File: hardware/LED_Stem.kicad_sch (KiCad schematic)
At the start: 4 parts

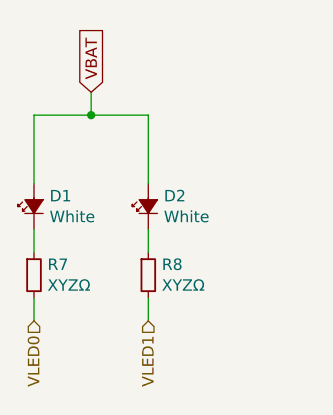
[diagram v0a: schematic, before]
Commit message: Fixed a bug, where I was sorting all the LEDs :S Removed all DRC rules Ready to fillet tracks
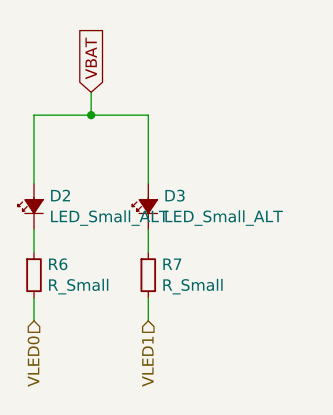
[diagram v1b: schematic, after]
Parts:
- D2: renamed from D1; value White -> LED_Small_ALT; footprint Snowflake:0603_LED_HandSolder -> Snowflake:0603_LED_HandSolder_No_Silk
- D3: renamed from D2; value White -> LED_Small_ALT; footprint Snowflake:0603_LED_HandSolder -> Snowflake:0603_LED_HandSolder_No_Silk
- R6: renamed from R7; value XYZΩ -> R_Small
- R7: renamed from R8; value XYZΩ -> R_Small
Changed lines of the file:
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@@
   (symbol (lib_id "Snowflake:LED_Small_ALT") (at 50.8 66.04 90) (unit 1)
     (in_bom yes) (on_board yes)
-    (property "Reference" "D1" (id 0) (at 52.5272 64.8716 90)
+    (property "Reference" "D2" (id 0) (at 52.5272 64.8716 90)
       (effects (font (size 1.27 1.27)) (justify right))
     )
-    (property "Value" "White" (id 1) (at 52.5272 67.183 90)
+    (property "Value" "LED_Small_ALT" (id 1) (at 52.5272 67.183 90)
       (effects (font (size 1.27 1.27)) (justify right))
     )
-    (property "Footprint" "Snowflake:0603_LED_HandSolder" (id 2) (at 50.8 66.04 90)
+    (property "Footprint" "Snowflake:0603_LED_HandSolder_No_Silk" (id 2) (at 50.8 66.04 90)
       (effects (font (size 1.27 1.27)) hide)
     )
@@
   (symbol (lib_id "Snowflake:R_Small") (at 50.8 73.66 0) (unit 1)
     (in_bom yes) (on_board yes)
-    (property "Reference" "R7" (id 0) (at 52.2986 72.4916 0)
+    (property "Reference" "R6" (id 0) (at 52.2986 72.4916 0)
       (effects (font (size 1.27 1.27)) (justify left))
     )
-    (property "Value" "XYZΩ" (id 1) (at 52.2986 74.803 0)
+    (property "Value" "R_Small" (id 1) (at 52.2986 74.803 0)
       (effects (font (size 1.27 1.27)) (justify left))
     )
@@
   (symbol (lib_id "Snowflake:LED_Small_ALT") (at 63.5 66.04 90) (unit 1)
     (in_bom yes) (on_board yes)
-    (property "Reference" "D2" (id 0) (at 65.2272 64.8716 90)
+    (property "Reference" "D3" (id 0) (at 65.2272 64.8716 90)
       (effects (font (size 1.27 1.27)) (justify right))
     )
-    (property "Value" "White" (id 1) (at 65.2272 67.183 90)
+    (property "Value" "LED_Small_ALT" (id 1) (at 65.2272 67.183 90)
       (effects (font (size 1.27 1.27)) (justify right))
     )
-    (property "Footprint" "Snowflake:0603_LED_HandSolder" (id 2) (at 63.5 66.04 90)
+    (property "Footprint" "Snowflake:0603_LED_HandSolder_No_Silk" (id 2) (at 63.5 66.04 90)
       (effects (font (size 1.27 1.27)) hide)
     )
@@
   (symbol (lib_id "Snowflake:R_Small") (at 63.5 73.66 0) (unit 1)
     (in_bom yes) (on_board yes)
-    (property "Reference" "R8" (id 0) (at 64.9986 72.4916 0)
+    (property "Reference" "R7" (id 0) (at 64.9986 72.4916 0)
       (effects (font (size 1.27 1.27)) (justify left))
     )
-    (property "Value" "XYZΩ" (id 1) (at 64.9986 74.803 0)
+    (property "Value" "R_Small" (id 1) (at 64.9986 74.803 0)
       (effects (font (size 1.27 1.27)) (justify left))
     )

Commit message: Discarded the idea of using AAA batteries and switched to CR2032s
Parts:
- D2, D3: footprint Snowflake:0603_LED_HandSolder_No_Silk -> Snowflake:4014_LED
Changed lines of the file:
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@@
       (effects (font (size 1.27 1.27)) (justify right))
     )
-    (property "Footprint" "Snowflake:0603_LED_HandSolder_No_Silk" (id 2) (at 50.8 66.04 90)
+    (property "Footprint" "Snowflake:4014_LED" (id 2) (at 50.8 66.04 90)
       (effects (font (size 1.27 1.27)) hide)
     )
@@
       (effects (font (size 1.27 1.27)) (justify right))
     )
-    (property "Footprint" "Snowflake:0603_LED_HandSolder_No_Silk" (id 2) (at 63.5 66.04 90)
+    (property "Footprint" "Snowflake:4014_LED" (id 2) (at 63.5 66.04 90)
       (effects (font (size 1.27 1.27)) hide)
     )

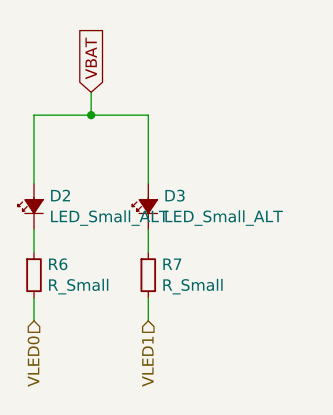
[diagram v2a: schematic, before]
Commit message: Pre-test push. Happy with the layout, waiting for the tests to choose an LED, resitor and battery holder
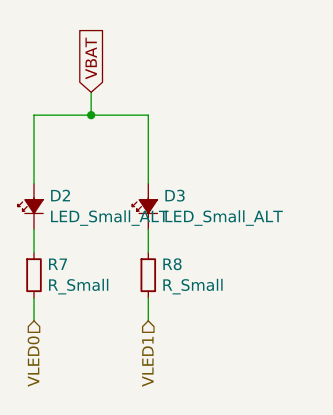
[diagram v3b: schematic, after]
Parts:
- renumbered R6 to R7, R7 to R8
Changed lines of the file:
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@@
   (symbol (lib_id "Snowflake:R_Small") (at 50.8 73.66 0) (unit 1)
     (in_bom yes) (on_board yes)
-    (property "Reference" "R6" (id 0) (at 52.2986 72.4916 0)
+    (property "Reference" "R7" (id 0) (at 52.2986 72.4916 0)
       (effects (font (size 1.27 1.27)) (justify left))
     )
@@
   (symbol (lib_id "Snowflake:R_Small") (at 63.5 73.66 0) (unit 1)
     (in_bom yes) (on_board yes)
-    (property "Reference" "R7" (id 0) (at 64.9986 72.4916 0)
+    (property "Reference" "R8" (id 0) (at 64.9986 72.4916 0)
       (effects (font (size 1.27 1.27)) (justify left))
     )

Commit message: Happy with the HW
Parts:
- R7, R8: footprint Snowflake:0805-R_Handsolder -> Snowflake:0805-R_Handsolder_NoSilk
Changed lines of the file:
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@@
       (effects (font (size 1.27 1.27)) (justify left))
     )
-    (property "Footprint" "Snowflake:0805-R_Handsolder" (id 2) (at 50.8 73.66 0)
+    (property "Footprint" "Snowflake:0805-R_Handsolder_NoSilk" (id 2) (at 50.8 73.66 0)
       (effects (font (size 1.27 1.27)) hide)
     )
@@
       (effects (font (size 1.27 1.27)) (justify left))
     )
-    (property "Footprint" "Snowflake:0805-R_Handsolder" (id 2) (at 63.5 73.66 0)
+    (property "Footprint" "Snowflake:0805-R_Handsolder_NoSilk" (id 2) (at 63.5 73.66 0)
       (effects (font (size 1.27 1.27)) hide)
     )

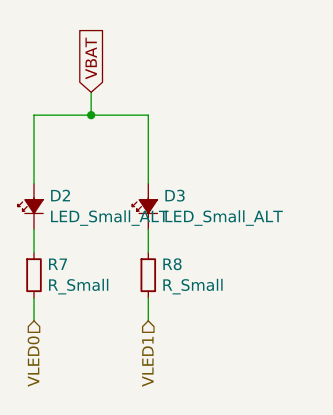
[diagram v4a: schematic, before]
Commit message: Updated footprint for LED as it was a bit off and changed to a single CR2032 holder that's quite compact
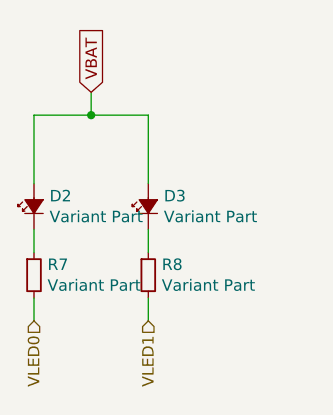
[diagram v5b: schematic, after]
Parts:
- D2, D3: value LED_Small_ALT -> Variant Part; footprint Snowflake:4014_LED -> Snowflake:4014_LED_HandSolder_NoSilk; Variant_Osram (none) -> 475-KWDCLMS2.EC-CXCZ-4L7M-1-20-R18CT-ND
- R7, R8: value R_Small -> Variant Part; Variant_Osram (none) -> CR0805-FX-56R0ELFCT-ND
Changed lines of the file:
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@@
       (effects (font (size 1.27 1.27)) (justify right))
     )
-    (property "Value" "LED_Small_ALT" (id 1) (at 52.5272 67.183 90)
+    (property "Value" "Variant Part" (id 1) (at 52.5272 67.183 90)
       (effects (font (size 1.27 1.27)) (justify right))
     )
-    (property "Footprint" "Snowflake:4014_LED" (id 2) (at 50.8 66.04 90)
+    (property "Footprint" "Snowflake:4014_LED_HandSolder_NoSilk" (id 2) (at 50.8 66.04 90)
       (effects (font (size 1.27 1.27)) hide)
     )
     (property "Datasheet" "~" (id 3) (at 50.8 66.04 90)
+      (effects (font (size 1.27 1.27)) hide)
+    )
+    (property "Variant_Osram" "475-KWDCLMS2.EC-CXCZ-4L7M-1-20-R18CT-ND" (id 4) (at 50.8 66.04 0)
       (effects (font (size 1.27 1.27)) hide)
     )
@@
       (effects (font (size 1.27 1.27)) (justify left))
     )
-    (property "Value" "R_Small" (id 1) (at 52.2986 74.803 0)
+    (property "Value" "Variant Part" (id 1) (at 52.2986 74.803 0)
       (effects (font (size 1.27 1.27)) (justify left))
     )
@@
     )
     (property "Datasheet" "~" (id 3) (at 50.8 73.66 0)
+      (effects (font (size 1.27 1.27)) hide)
+    )
+    (property "Variant_Osram" "CR0805-FX-56R0ELFCT-ND" (id 4) (at 50.8 73.66 0)
       (effects (font (size 1.27 1.27)) hide)
     )
@@
       (effects (font (size 1.27 1.27)) (justify right))
     )
-    (property "Value" "LED_Small_ALT" (id 1) (at 65.2272 67.183 90)
+    (property "Value" "Variant Part" (id 1) (at 65.2272 67.183 90)
       (effects (font (size 1.27 1.27)) (justify right))
     )
-    (property "Footprint" "Snowflake:4014_LED" (id 2) (at 63.5 66.04 90)
+    (property "Footprint" "Snowflake:4014_LED_HandSolder_NoSilk" (id 2) (at 63.5 66.04 90)
       (effects (font (size 1.27 1.27)) hide)
     )
     (property "Datasheet" "~" (id 3) (at 63.5 66.04 90)
+      (effects (font (size 1.27 1.27)) hide)
+    )
+    (property "Variant_Osram" "475-KWDCLMS2.EC-CXCZ-4L7M-1-20-R18CT-ND" (id 4) (at 63.5 66.04 0)
       (effects (font (size 1.27 1.27)) hide)
     )
@@
       (effects (font (size 1.27 1.27)) (justify left))
     )
-    (property "Value" "R_Small" (id 1) (at 64.9986 74.803 0)
+    (property "Value" "Variant Part" (id 1) (at 64.9986 74.803 0)
       (effects (font (size 1.27 1.27)) (justify left))
     )
@@
       (effects (font (size 1.27 1.27)) hide)
     )
+    (property "Variant_Osram" "CR0805-FX-56R0ELFCT-ND" (id 4) (at 63.5 73.66 0)
+      (effects (font (size 1.27 1.27)) hide)
+    )

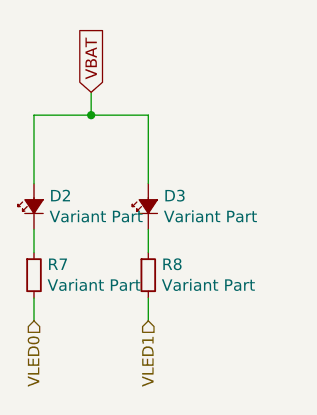
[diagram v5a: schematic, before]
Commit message: Changed a couple of parts to alternatives that are more available AND cheaper
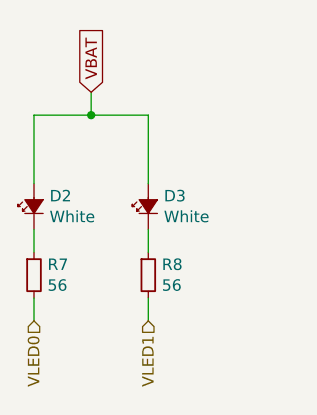
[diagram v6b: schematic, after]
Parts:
- D2, D3: value Variant Part -> White; Digikey PN (none) -> 475-KWDCLMS2.EC-CXCZ-4L7M-1-20-R18CT-ND; MPN (none) -> KWDCLMS2.EC-CXCZ-4L7M; Manufacturer (none) -> Osram; Package (none) -> 4014; Variant_Osram 475-KWDCLMS2.EC-CXCZ-4L7M-1-20-R18CT-ND -> (none)
- R7, R8: value Variant Part -> 56; Digikey PN (none) -> 311-56ARCT-ND; MPN (none) -> RC0805FR-1056RL; Manufacturer (none) -> Yageo; Package (none) -> 0805; Tolerance (none) -> ±1%; Variant_Osram CR0805-FX-56R0ELFCT-ND -> (none)
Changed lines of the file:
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@@
       (effects (font (size 1.27 1.27)) (justify right))
     )
-    (property "Value" "Variant Part" (id 1) (at 52.5272 67.183 90)
+    (property "Value" "White" (id 1) (at 52.5272 67.183 90)
       (effects (font (size 1.27 1.27)) (justify right))
     )
@@
       (effects (font (size 1.27 1.27)) hide)
     )
-    (property "Variant_Osram" "475-KWDCLMS2.EC-CXCZ-4L7M-1-20-R18CT-ND" (id 4) (at 50.8 66.04 0)
+    (property "Variant_Osram" "" (id 4) (at 50.8 66.04 0)
+      (effects (font (size 1.27 1.27)) hide)
+    )
+    (property "Package" "4014" (id 5) (at 50.8 66.04 0)
+      (effects (font (size 1.27 1.27)) hide)
+    )
+    (property "Digikey PN" "475-KWDCLMS2.EC-CXCZ-4L7M-1-20-R18CT-ND" (id 6) (at 50.8 66.04 0)
+      (effects (font (size 1.27 1.27)) hide)
+    )
+    (property "MPN" "KWDCLMS2.EC-CXCZ-4L7M" (id 7) (at 50.8 66.04 0)
+      (effects (font (size 1.27 1.27)) hide)
+    )
+    (property "Manufacturer" "Osram" (id 8) (at 50.8 66.04 0)
       (effects (font (size 1.27 1.27)) hide)
     )
@@
       (effects (font (size 1.27 1.27)) (justify left))
     )
-    (property "Value" "Variant Part" (id 1) (at 52.2986 74.803 0)
+    (property "Value" "56" (id 1) (at 52.2986 74.803 0)
       (effects (font (size 1.27 1.27)) (justify left))
     )
@@
       (effects (font (size 1.27 1.27)) hide)
     )
-    (property "Variant_Osram" "CR0805-FX-56R0ELFCT-ND" (id 4) (at 50.8 73.66 0)
+    (property "Variant_Osram" "" (id 4) (at 50.8 73.66 0)
+      (effects (font (size 1.27 1.27)) hide)
+    )
+    (property "Package" "0805" (id 5) (at 50.8 73.66 0)
+      (effects (font (size 1.27 1.27)) hide)
+    )
+    (property "Tolerance" "±1%" (id 6) (at 50.8 73.66 0)
+      (effects (font (size 1.27 1.27)) hide)
+    )
+    (property "Digikey PN" "311-56ARCT-ND" (id 7) (at 50.8 73.66 0)
+      (effects (font (size 1.27 1.27)) hide)
+    )
+    (property "MPN" "RC0805FR-1056RL" (id 8) (at 50.8 73.66 0)
+      (effects (font (size 1.27 1.27)) hide)
+    )
+    (property "Manufacturer" "Yageo" (id 9) (at 50.8 73.66 0)
       (effects (font (size 1.27 1.27)) hide)
     )
@@
       (effects (font (size 1.27 1.27)) (justify right))
     )
-    (property "Value" "Variant Part" (id 1) (at 65.2272 67.183 90)
+    (property "Value" "White" (id 1) (at 65.2272 67.183 90)
       (effects (font (size 1.27 1.27)) (justify right))
     )
@@
       (effects (font (size 1.27 1.27)) hide)
     )
-    (property "Variant_Osram" "475-KWDCLMS2.EC-CXCZ-4L7M-1-20-R18CT-ND" (id 4) (at 63.5 66.04 0)
+    (property "Variant_Osram" "" (id 4) (at 63.5 66.04 0)
+      (effects (font (size 1.27 1.27)) hide)
+    )
+    (property "Package" "4014" (id 5) (at 63.5 66.04 0)
+      (effects (font (size 1.27 1.27)) hide)
+    )
+    (property "Digikey PN" "475-KWDCLMS2.EC-CXCZ-4L7M-1-20-R18CT-ND" (id 6) (at 63.5 66.04 0)
+      (effects (font (size 1.27 1.27)) hide)
+    )
+    (property "MPN" "KWDCLMS2.EC-CXCZ-4L7M" (id 7) (at 63.5 66.04 0)
+      (effects (font (size 1.27 1.27)) hide)
+    )
+    (property "Manufacturer" "Osram" (id 8) (at 63.5 66.04 0)
       (effects (font (size 1.27 1.27)) hide)
     )
@@
       (effects (font (size 1.27 1.27)) (justify left))
     )
-    (property "Value" "Variant Part" (id 1) (at 64.9986 74.803 0)
+    (property "Value" "56" (id 1) (at 64.9986 74.803 0)
       (effects (font (size 1.27 1.27)) (justify left))
     )
@@
       (effects (font (size 1.27 1.27)) hide)
     )
-    (property "Variant_Osram" "CR0805-FX-56R0ELFCT-ND" (id 4) (at 63.5 73.66 0)
+    (property "Variant_Osram" "" (id 4) (at 63.5 73.66 0)
       (effects (font (size 1.27 1.27)) hide)
     )
+    (property "Package" "0805" (id 5) (at 63.5 73.66 0)
+      (effects (font (size 1.27 1.27)) hide)
+    )
+    (property "Tolerance" "±1%" (id 6) (at 63.5 73.66 0)
+      (effects (font (size 1.27 1.27)) hide)
+    )
+    (property "Digikey PN" "311-56ARCT-ND" (id 7) (at 63.5 73.66 0)
+      (effects (font (size 1.27 1.27)) hide)
+    )
+    (property "MPN" "RC0805FR-1056RL" (id 8) (at 63.5 73.66 0)
+      (effects (font (size 1.27 1.27)) hide)
+    )
+    (property "Manufacturer" "Yageo" (id 9) (at 63.5 73.66 0)
+      (effects (font (size 1.27 1.27)) hide)
+    )

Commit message: v1.0.0 First manufactured version Updated gitignore and removed a bunch of virtualenv files Tweaked some footprints Added farnell PN, MPNs, etc.
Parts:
- D2, D3: Farnell PN (none) -> 3625384
- R7, R8: Farnell PN (none) -> 9237330
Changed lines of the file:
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@@
+      (effects (font (size 1.27 1.27)) hide)
+    )
+    (property "Farnell PN" "3625384" (id 9) (at 50.8 66.04 0)
       (effects (font (size 1.27 1.27)) hide)
     )
@@
       (effects (font (size 1.27 1.27)) hide)
     )
+    (property "Farnell PN" "9237330" (id 10) (at 50.8 73.66 0)
+      (effects (font (size 1.27 1.27)) hide)
+    )
     (pin "1")
     (pin "2")
@@
     )
     (property "Manufacturer" "Osram" (id 8) (at 63.5 66.04 0)
+      (effects (font (size 1.27 1.27)) hide)
+    )
+    (property "Farnell PN" "3625384" (id 9) (at 63.5 66.04 0)
       (effects (font (size 1.27 1.27)) hide)
     )
@@
       (effects (font (size 1.27 1.27)) hide)
     )
+    (property "Farnell PN" "9237330" (id 10) (at 63.5 73.66 0)
+      (effects (font (size 1.27 1.27)) hide)
+    )

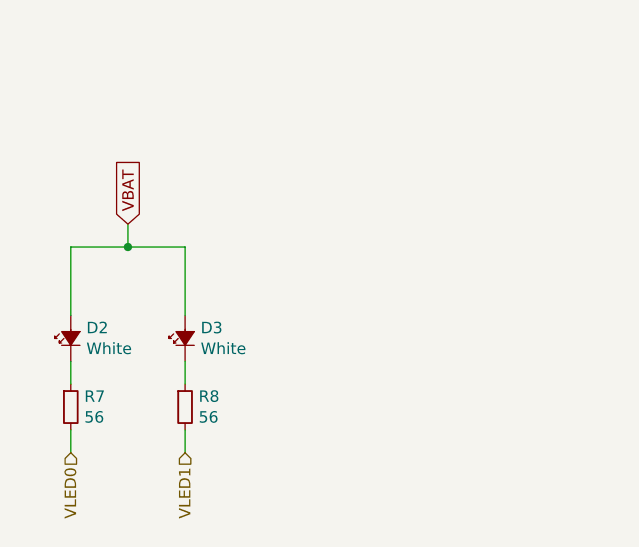
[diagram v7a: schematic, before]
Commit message: Added some text to the sheet to commit hash and date printed on the outputs
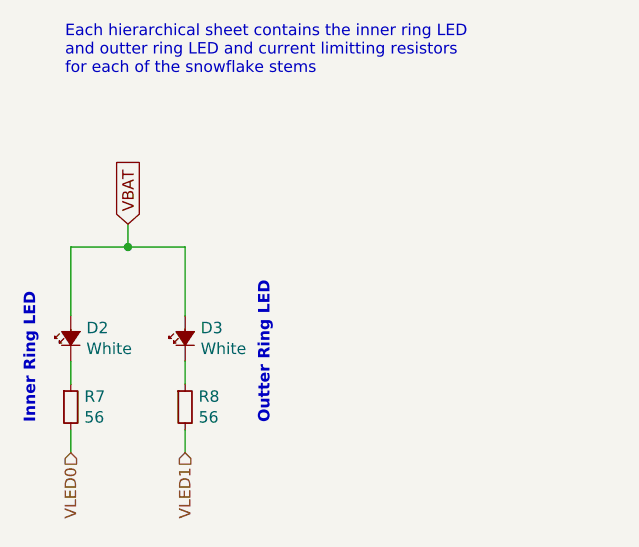
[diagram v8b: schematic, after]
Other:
- note added: "Each hierarchical sheet contains the inner ring LED and outter ring LED and current limitting resistors for each of the snowflake stems"
- note added: "Inner Ring LED"
- note added: "Outter Ring LED"
- title: (none) -> Snowflake
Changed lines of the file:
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@@
 (kicad_sch (version 20211123) (generator eeschema)
   (paper "A4")
+  (title_block
+    (title "Snowflake")
+    (date "${TODAY}")
+    (rev "1.0.0")
+    (comment 1 "Docs Generated from commit ${GIT_HASH}")
+  )
   (junction (at 57.15 55.88) (diameter 0) (color 0 0 0 0)
   )
@@
     (stroke (width 0) (type default) (color 0 0 0 0))
   )
+  (text "Outter Ring LED" (at 73.025 75.565 90)
+    (effects (font (size 1.27 1.27) bold) (justify left bottom))
+  )
+  (text "Inner Ring LED" (at 46.99 75.565 90)
+    (effects (font (size 1.27 1.27) bold) (justify left bottom))
+  )
+  (text "Each hierarchical sheet contains the inner ring LED\nand outter ring LED and current limitting resistors\nfor each of the snowflake stems"
+    (at 50.165 36.83 0)
+    (effects (font (size 1.27 1.27)) (justify left bottom))
+  )
   (global_label "VBAT" (shape input) (at 57.15 53.34 90) (fields_autoplaced)
